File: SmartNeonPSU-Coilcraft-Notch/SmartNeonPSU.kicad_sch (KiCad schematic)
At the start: 87 parts, among them J1 12VDC, J2 POWER, J3 SERIAL+GPIO, J4 TPS_IO, J5 EXT_SW, J6 LAMP1+, J7 LAMP1-, Q1 MMSS8050, Q2 MMSS8050, Q3 IRF7303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

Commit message: v2
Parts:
- removed H5: MountingHole_Pad, MountingHole:MountingHole_3.2mm_M3_Pad_Via, symbol Mechanical:MountingHole_Pad
- removed J1: 12VDC, Connector_BarrelJack:BarrelJack_Horizontal, symbol Connector:Barrel_Jack_Switch
- removed SW3: CONTROL, SmartNeonPSU:E-Switch_R1966A‎_7mm_RA, symbol Switch:SW_SPDT_MSM
- renumbered J2 to J1, J3 to J2, J4 to J3, J5 to J4, J6 to J5, J7 to J6
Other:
- note removed: "External Switch"
- moved on the sheet: J1

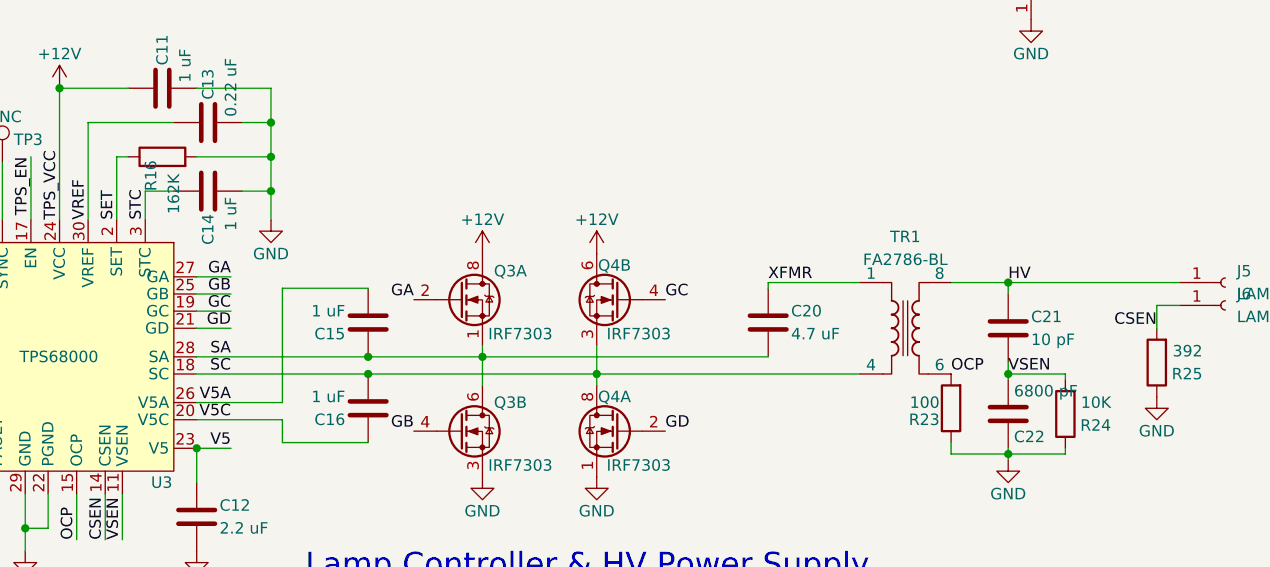
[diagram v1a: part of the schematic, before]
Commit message: Add docs, sync schematics with reality
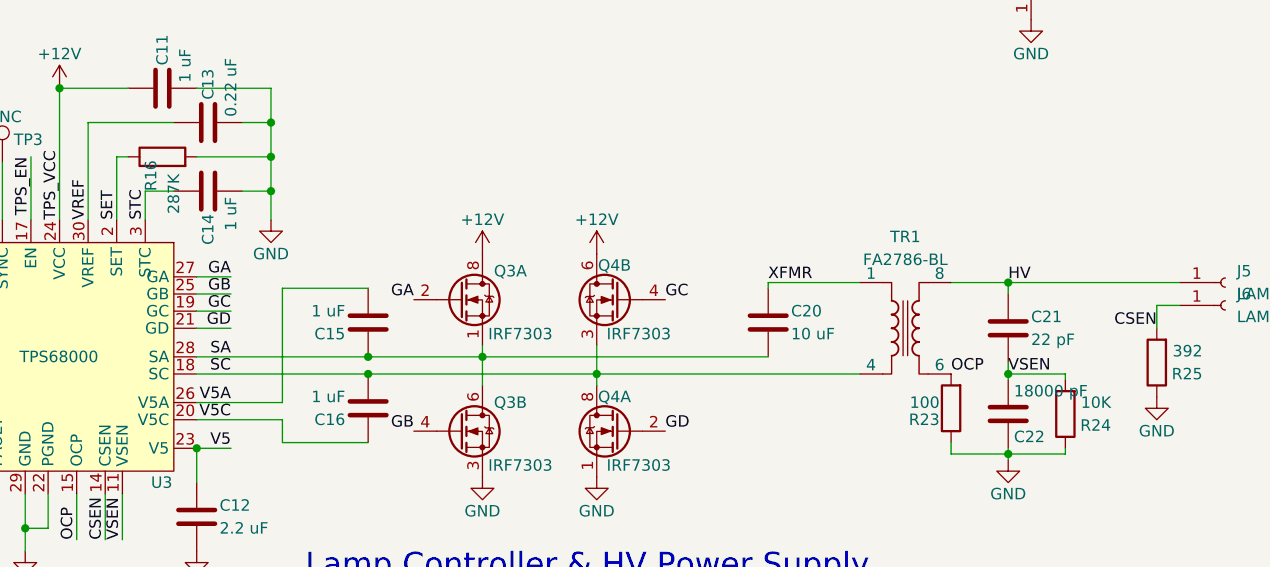
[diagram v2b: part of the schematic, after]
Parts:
- C20: value 4.7 uF -> 10 uF; MPN1 C2012X7R1H475K125AE -> C2012X5R1V106K085AC
- C21: value 10 pF -> 22 pF; MPN1 C4520C0G3F100F -> C4520C0G3F220K
- C22: value 6800 pF -> 18000 pF; MPN1 CC0805KRX7R9BB682 -> CC0805KRX7R9BB183
- R16: value 162K -> 287K; MPN1 RC0805FR-07162KL -> RC0805FR-07287KL
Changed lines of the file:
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@@
       (effects (font (size 1.27 1.27)) (justify left))
     )
-    (property "Value" "10 pF" (id 1) (at 253.365 133.35 0)
+    (property "Value" "22 pF" (id 1) (at 253.365 133.35 0)
       (effects (font (size 1.27 1.27)) (justify left))
     )
@@
       (effects (font (size 1.27 1.27)) hide)
     )
-    (property "MPN1" "C4520C0G3F100F" (id 4) (at 250.825 132.08 0)
+    (property "MPN1" "C4520C0G3F220K" (id 4) (at 250.825 132.08 0)
       (effects (font (size 1.27 1.27)) hide)
     )
@@
       (effects (font (size 1.27 1.27)) (justify left))
     )
-    (property "Value" "6800 pF" (id 1) (at 251.46 139.065 0)
+    (property "Value" "18000 pF" (id 1) (at 251.46 139.065 0)
       (effects (font (size 1.27 1.27)) (justify left))
     )
@@
       (effects (font (size 1.27 1.27)) hide)
     )
-    (property "MPN1" "CC0805KRX7R9BB682" (id 4) (at 250.825 141.605 0)
+    (property "MPN1" "CC0805KRX7R9BB183" (id 4) (at 250.825 141.605 0)
       (effects (font (size 1.27 1.27)) hide)
     )
@@
       (effects (font (size 1.27 1.27)) (justify left))
     )
-    (property "Value" "162K" (id 1) (at 158.115 119.38 0)
+    (property "Value" "287K" (id 1) (at 158.115 119.38 0)
       (effects (font (size 1.27 1.27)) (justify left))
     )
@@
       (effects (font (size 1.27 1.27)) hide)
     )
-    (property "MPN1" "RC0805FR-07162KL" (id 4) (at 156.845 113.03 0)
+    (property "MPN1" "RC0805FR-07287KL" (id 4) (at 156.845 113.03 0)
       (effects (font (size 1.27 1.27)) hide)
     )
@@
     )
     (pin "1")
-  )
-  (symbol (lib_id "Device:C") (at 224.155 131.445 0) (unit 1)
-    (in_bom yes) (on_board yes)
-    (property "Reference" "C20" (id 0) (at 226.695 130.175 0)
-      (effects (font (size 1.27 1.27)) (justify left))
-    )
-    (property "Value" "4.7 uF" (id 1) (at 226.695 132.715 0)
-      (effects (font (size 1.27 1.27)) (justify left))
-    )
-    (property "Footprint" "Capacitor_SMD:C_0805_2012Metric" (id 2) (at 225.1202 135.255 0)
-      (effects (font (size 1.27 1.27)) hide)
-    )
-    (property "Datasheet" "~" (id 3) (at 224.155 131.445 0)
-      (effects (font (size 1.27 1.27)) hide)
-    )
-    (property "MPN1" "C2012X7R1H475K125AE" (id 4) (at 224.155 131.445 0)
-      (effects (font (size 1.27 1.27)) hide)
-    )
-    (pin "1")
-    (pin "2")
   )
   (symbol (lib_id "Device:R") (at 71.628 139.7144 180) (unit 1)
@@
     (pin "7")
     (pin "8")
+  )
+  (symbol (lib_id "Device:C") (at 224.155 131.445 0) (unit 1)
+    (in_bom yes) (on_board yes)
+    (property "Reference" "C20" (id 0) (at 226.695 130.175 0)
+      (effects (font (size 1.27 1.27)) (justify left))
+    )
+    (property "Value" "10 uF" (id 1) (at 226.695 132.715 0)
+      (effects (font (size 1.27 1.27)) (justify left))
+    )
+    (property "Footprint" "Capacitor_SMD:C_0805_2012Metric" (id 2) (at 225.1202 135.255 0)
+      (effects (font (size 1.27 1.27)) hide)
+    )
+    (property "Datasheet" "~" (id 3) (at 224.155 131.445 0)
+      (effects (font (size 1.27 1.27)) hide)
+    )
+    (property "MPN1" "C2012X5R1V106K085AC" (id 4) (at 224.155 131.445 0)
+      (effects (font (size 1.27 1.27)) hide)
+    )
+    (pin "1")
+    (pin "2")
   )
   (symbol (lib_id "Device:R") (at 179.07 82.55 270) (unit 1)
@@
       (reference "C19") (unit 1) (value "47 uF") (footprint "Capacitor_SMD:C_0805_2012Metric")
     )
-    (path "/aa213ca8-3e06-4412-af52-3386c4fab9f9"
-      (reference "C20") (unit 1) (value "4.7 uF") (footprint "Capacitor_SMD:C_0805_2012Metric")
+    (path "/b3a83011-8a4f-4104-87e0-2ae5afbb7d0a"
+      (reference "C20") (unit 1) (value "10 uF") (footprint "Capacitor_SMD:C_0805_2012Metric")
     )
     (path "/449e3155-16ea-42e5-8b6a-0c318fc89476"
-      (reference "C21") (unit 1) (value "10 pF") (footprint "Capacitor_SMD:C_1808_4520Metric_Slot")
+      (reference "C21") (unit 1) (value "22 pF") (footprint "Capacitor_SMD:C_1808_4520Metric_Slot")
     )
     (path "/51b8c561-e459-4fac-a380-3761f1257871"
-      (reference "C22") (unit 1) (value "6800 pF") (footprint "Capacitor_SMD:C_0805_2012Metric")
+      (reference "C22") (unit 1) (value "18000 pF") (footprint "Capacitor_SMD:C_0805_2012Metric")
     )
     (path "/bc1c377b-a155-474a-a038-dbd44a4e7dd6"
@@
     )
     (path "/9a45920d-217a-4a92-b6c2-ecc141d16559"
-      (reference "R16") (unit 1) (value "162K") (footprint "Resistor_SMD:R_0805_2012Metric")
+      (reference "R16") (unit 1) (value "287K") (footprint "Resistor_SMD:R_0805_2012Metric")
     )
     (path "/097b057b-6f92-4820-a5b5-7281e3dc927b"
